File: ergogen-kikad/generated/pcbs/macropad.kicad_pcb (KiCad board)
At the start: 2 copper layers, 73.6 x 60.5 mm, 13 parts

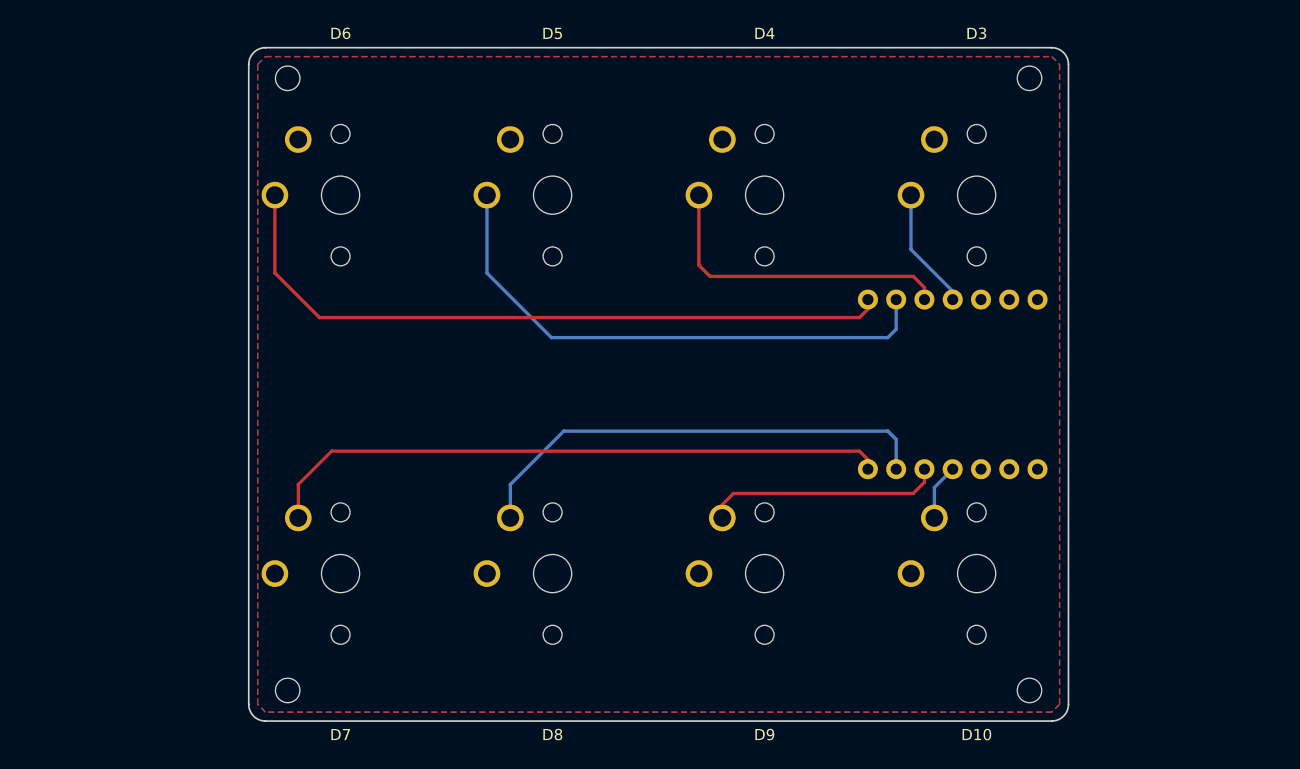
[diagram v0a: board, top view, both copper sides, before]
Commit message: Compact key rows and add controller-side keys through Ergogen
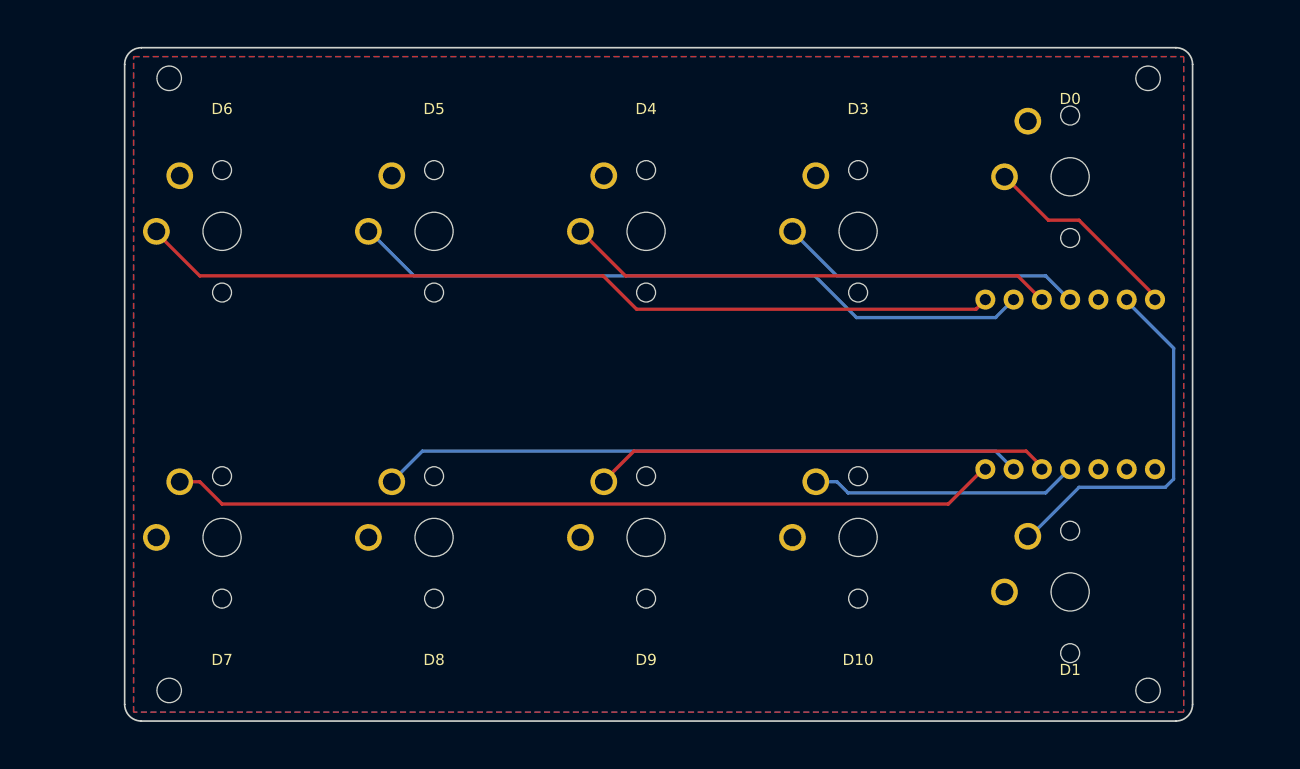
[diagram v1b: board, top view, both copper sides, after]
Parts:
- added S10: Choc v1 1U, PG1350_1U, F.Cu at (247.0, 167.2)
- added S9: Choc v1 1U, PG1350_1U, F.Cu at (247.0, 129.8)
- moved S1 11.1 mm to (170.8, 134.8)
- moved S2 11.1 mm to (189.8, 134.8)
- moved S3 11.1 mm to (208.9, 134.8)
- moved S5 11.1 mm to (170.8, 162.2)
- moved S6 11.1 mm to (189.8, 162.2)
- moved S7 11.1 mm to (208.9, 162.2)
- moved S4 11.1 mm to (227.9, 134.8)
- moved S8 11.1 mm to (227.9, 162.2)
- moved H1 10.7 mm to (166.0, 121.0)
- moved H2 10.7 mm to (254.0, 121.0)
- moved H3 10.7 mm to (166.0, 176.0)
- moved H4 10.7 mm to (254.0, 176.0)
- moved MCU1 10.5 mm to (247.0, 148.5)
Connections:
- MCU1 pad 1: (no net) -> D0
- MCU1 pad 2: (no net) -> D1
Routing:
- net D1: track 0.00 -> 33.2 mm
- net D9: track 21.4 -> 41.4 mm
- net D10: track 5.06 -> 24.6 mm
- net D0: track 0.00 -> 18.7 mm
- net D7: track 56.6 -> 74.6 mm
- net D3: track 10.9 -> 27.7 mm
- net D4: track 28.5 -> 44.3 mm
- net D8: track 42.6 -> 57.7 mm
- net D6: track 63.1 -> 78.0 mm
- net D5: track 49.2 -> 61.9 mm
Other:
- board size 73.6 x 60.5 mm -> 96 x 60.5 mm

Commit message: Align fifth-column caps with outer row edges
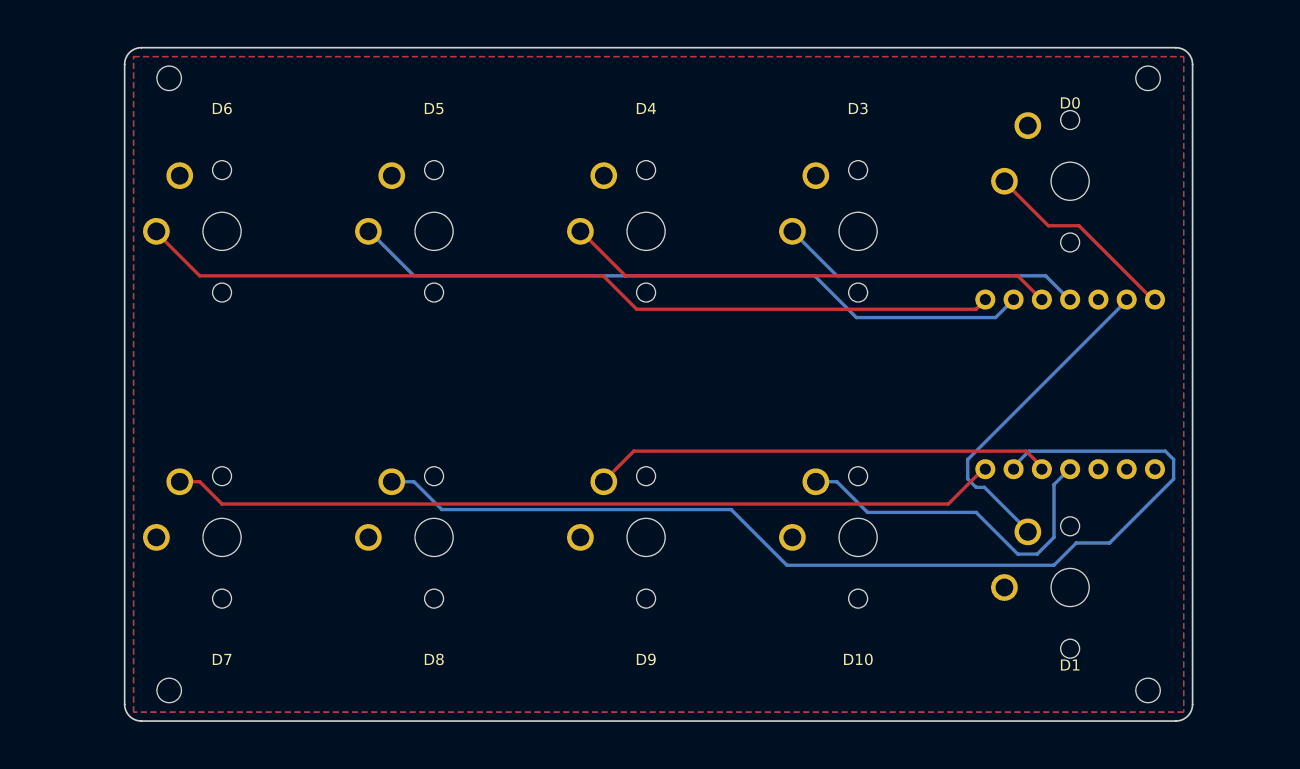
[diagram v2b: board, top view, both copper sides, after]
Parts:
- moved S10 0.40 mm to (247.0, 166.8)
- moved S9 0.40 mm to (247.0, 130.2)
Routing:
- net D8: track 57.7 -> 93.9 mm
- net D10: track 24.6 -> 31.9 mm
- net D1: track 33.2 -> 29.6 mm
- net D0: track 18.7 -> 18.1 mm

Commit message: Move mounts between switches and trim the board border
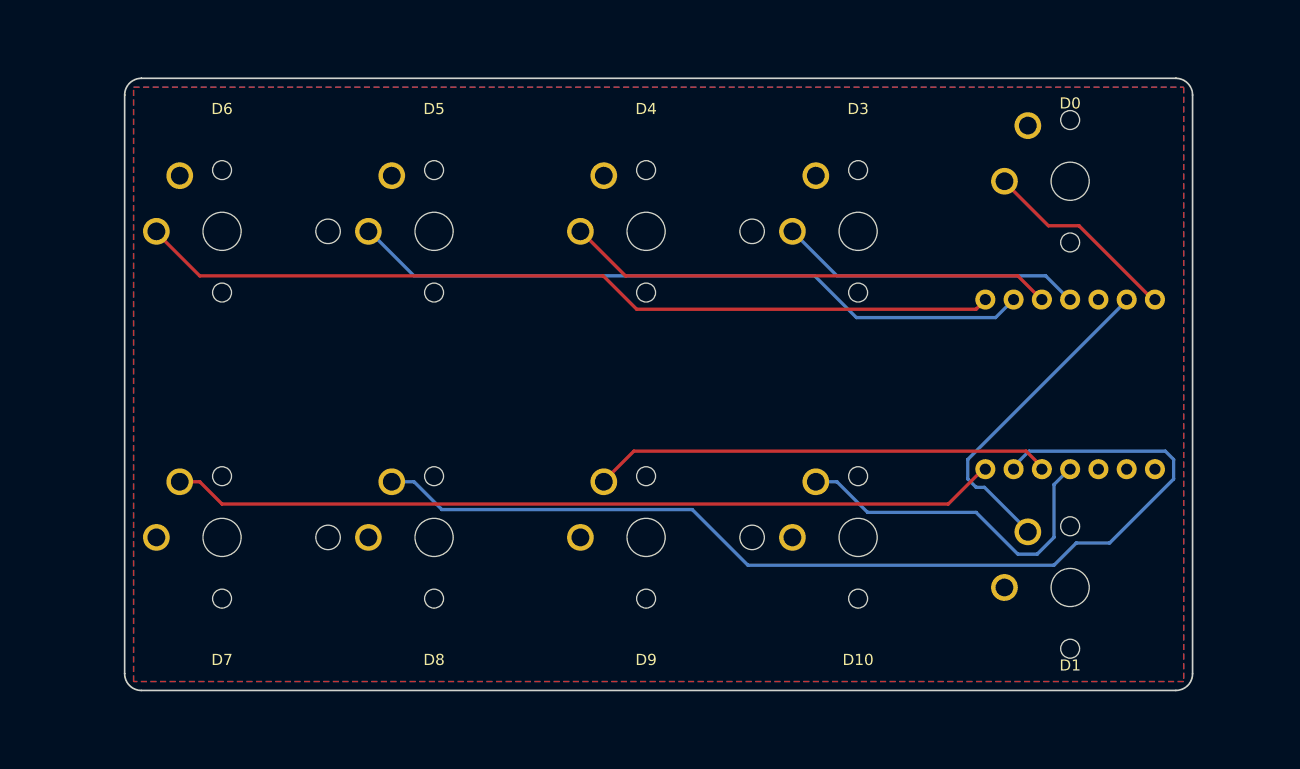
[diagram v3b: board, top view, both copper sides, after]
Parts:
- moved H2 38.1 mm to (218.4, 134.8)
- moved H4 38.1 mm to (218.4, 162.2)
- moved H1 19.8 mm to (180.3, 134.8)
- moved H3 19.8 mm to (180.3, 162.2)
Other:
- board size 96 x 60.5 mm -> 96 x 55 mm

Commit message: Add compact stacked memory LCD and regenerate matching carrier
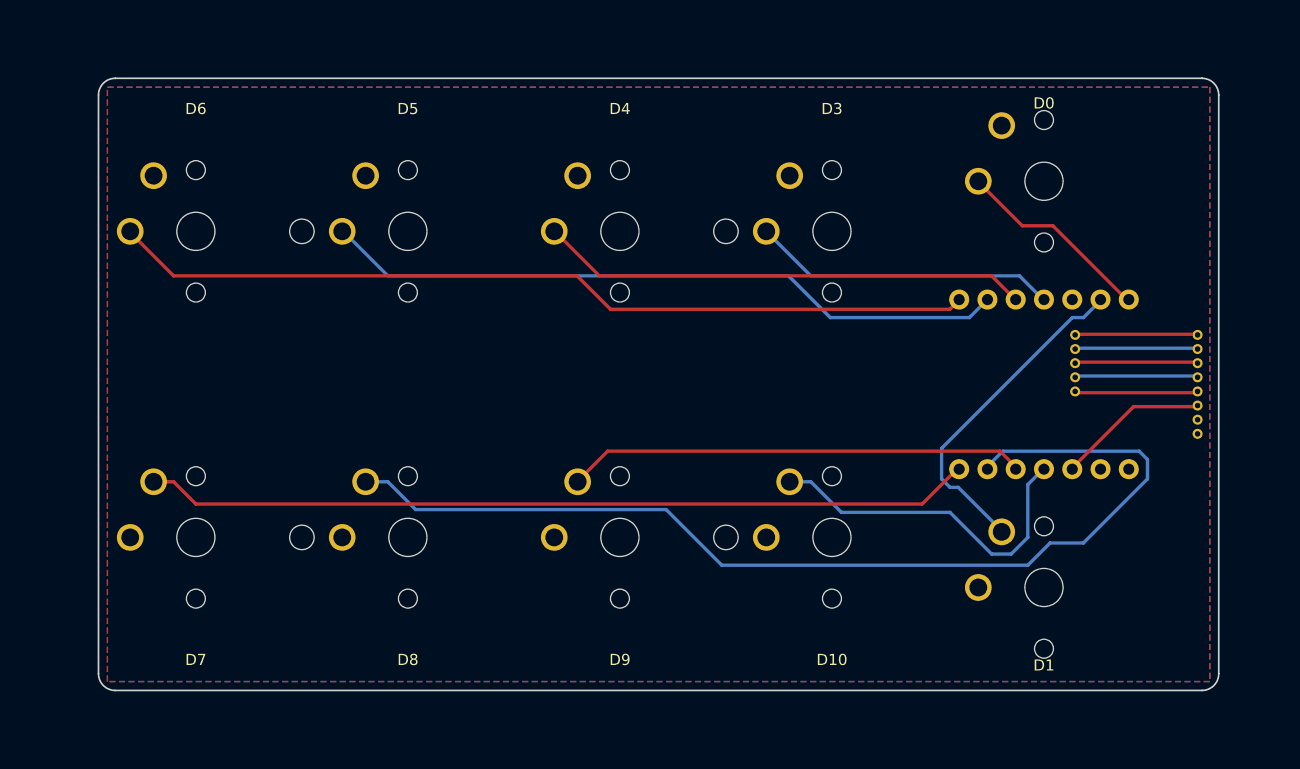
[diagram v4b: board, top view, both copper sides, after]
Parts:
- added LCD1: JDI LPM009M360A, JDI_LPM009M360A_Stack, F.Cu at (247.1, 148.5)
- added W1: Plus underside jumpers, XIAO_Plus_Underside_Wires, F.Cu at (247.4, 144.1)
- MCU1: value XIAO nRF52840 -> XIAO nRF52840 Plus
- moved H1 2.35 mm to (177.9, 134.8)
- moved H3 2.35 mm to (177.9, 162.2)
- moved S4 2.35 mm to (225.6, 134.8)
- moved S8 2.35 mm to (225.6, 162.2)
- moved H2 2.35 mm to (216.1, 134.8)
- moved H4 2.35 mm to (216.1, 162.2)
- moved MCU1 2.35 mm to (244.6, 148.5)
- moved S1 2.35 mm to (168.4, 134.8)
- moved S10 2.35 mm to (244.6, 166.8)
- moved S2 2.35 mm to (187.5, 134.8)
- moved S3 2.35 mm to (206.5, 134.8)
- moved S5 2.35 mm to (168.4, 162.2)
- moved S6 2.35 mm to (187.5, 162.2)
- moved S7 2.35 mm to (206.5, 162.2)
- moved S9 2.35 mm to (244.6, 130.2)
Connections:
- MCU1 pad 12: (no net) -> 3V3
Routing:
- net 3V3: track 0.00 -> 13.7 mm
- net LCD_EN: track 0.00 -> 11.2 mm
- net LCD_COM: track 0.00 -> 11.2 mm
- net LCD_CS: track 0.00 -> 11.2 mm
- net LCD_SI: track 0.00 -> 11.1 mm
- net LCD_CLK: track 0.00 -> 11.1 mm
- net D1: track 29.6 -> 30.2 mm
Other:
- board size 96 x 55 mm -> 100.6 x 55 mm

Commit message: Replace bare LCD with through-hole nice!view and nice!nano modules
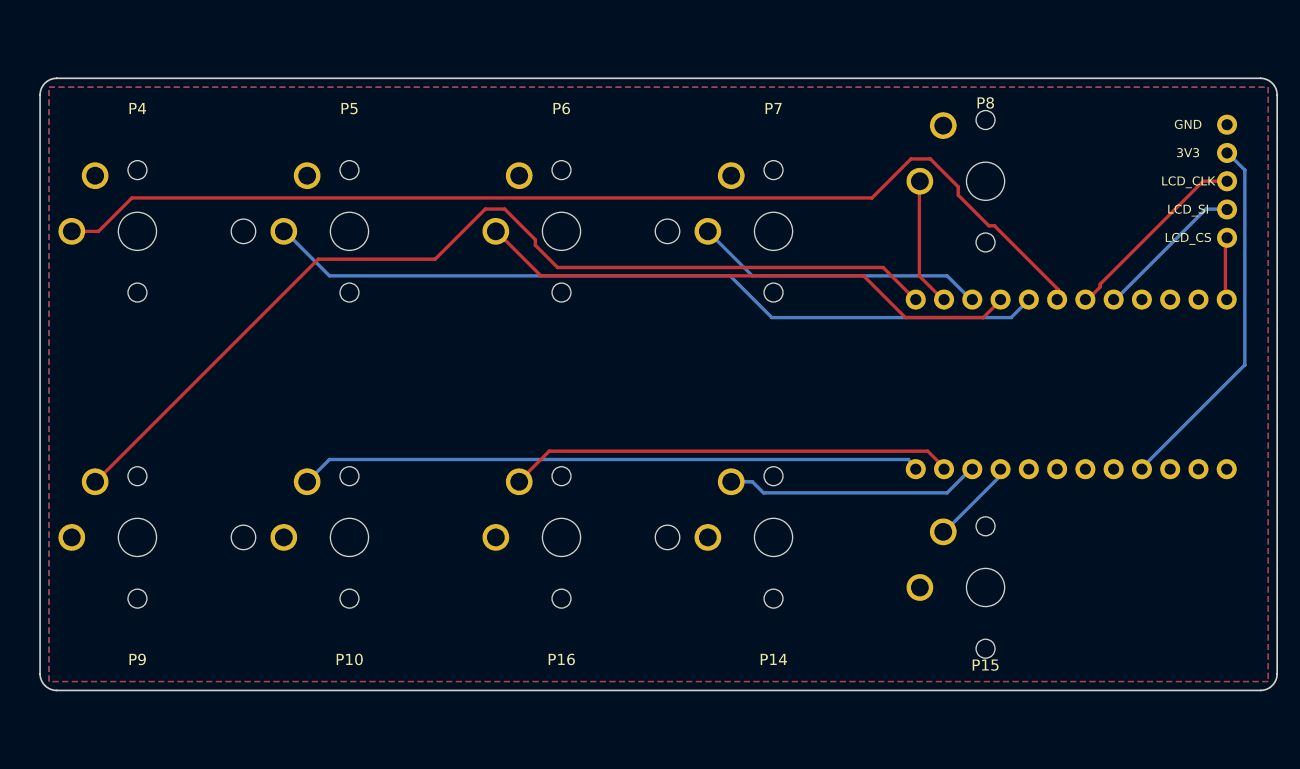
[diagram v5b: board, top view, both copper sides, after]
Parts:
- removed W1: Plus underside jumpers, XIAO_Plus_Underside_Wires
- LCD1: value JDI LPM009M360A -> nice!view; footprint JDI_LPM009M360A_Stack -> Nice_View_Wired_Module
- MCU1: value XIAO nRF52840 Plus -> nice!nano v2; footprint Seeed_XIAO_nRF52840 -> Nice_Nano_V2
- moved H1 5.25 mm to (172.7, 134.8)
- moved H2 5.25 mm to (210.8, 134.8)
- moved H3 5.25 mm to (172.7, 162.2)
- moved H4 5.25 mm to (210.8, 162.2)
- moved S1 5.25 mm to (163.2, 134.8)
- moved S10 5.25 mm to (239.4, 166.8)
- moved S2 5.25 mm to (182.2, 134.8)
- moved S3 5.25 mm to (201.3, 134.8)
- moved S4 5.25 mm to (220.3, 134.8)
- moved S5 5.25 mm to (163.2, 162.2)
- moved S6 5.25 mm to (182.2, 162.2)
- moved S7 5.25 mm to (201.3, 162.2)
- moved S8 5.25 mm to (220.3, 162.2)
- moved S9 5.25 mm to (239.4, 130.2)
- moved MCU1 2.45 mm to (247.1, 148.5)
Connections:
- net D6 renamed P4
- LCD1 pad 1: LCD_CLK -> GND
- LCD1 pad 2: LCD_SI -> 3V3
- LCD1 pad 3: LCD_CS -> LCD_CLK
- LCD1 pad 4: LCD_COM -> LCD_SI
- LCD1 pad 5: LCD_EN -> LCD_CS
- MCU1 pad 1: D0 -> LCD_CS
- MCU1 pad 10: D9 -> P7
- MCU1 pad 11: D10 -> P8
- MCU1 pad 12: 3V3 -> P9
- MCU1 pad 13: GND -> P10
- MCU1 pad 14: (no net) -> P16
- MCU1 pad 2: D1 -> (no net)
- MCU1 pad 3: (no net) -> GND
- MCU1 pad 4: D3 -> GND
- MCU1 pad 5: D4 -> LCD_SI
- MCU1 pad 6: D5 -> LCD_CLK
- MCU1 pad 8: D7 -> P5
- MCU1 pad 9: D8 -> P6
- S10 pad 1: D1 -> P15
- S2 pad 2: D5 -> P5
- S3 pad 2: D4 -> P6
- S4 pad 2: D3 -> P7
- S5 pad 1: D7 -> P9
- S6 pad 1: D8 -> P10
- S7 pad 1: D9 -> P16
- S8 pad 1: D10 -> P14
- S9 pad 2: D0 -> P8
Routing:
- net D8: track 93.9 -> 0.00 mm
- net P9: track 0.00 -> 87.8 mm
- net D7: track 74.6 -> 0.00 mm
- net P5: track 0.00 -> 70.8 mm
- net D5: track 61.9 -> 0.00 mm
- net P10: track 0.00 -> 56.0 mm
- net P6: track 0.00 -> 49.3 mm
- net D4: track 44.3 -> 0.00 mm
- net D9: track 41.4 -> 0.00 mm
- net P16: track 0.00 -> 40.2 mm
- net D10: track 31.9 -> 0.00 mm
- net D1: track 30.2 -> 0.00 mm
- net D3: track 27.7 -> 0.00 mm
- net P7: track 0.00 -> 26.5 mm
- net P14: track 0.00 -> 23.3 mm
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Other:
- board size 100.6 x 55 mm -> 111.1 x 55 mm

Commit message: Use landscape fifth-column caps and add right-side mounting pair
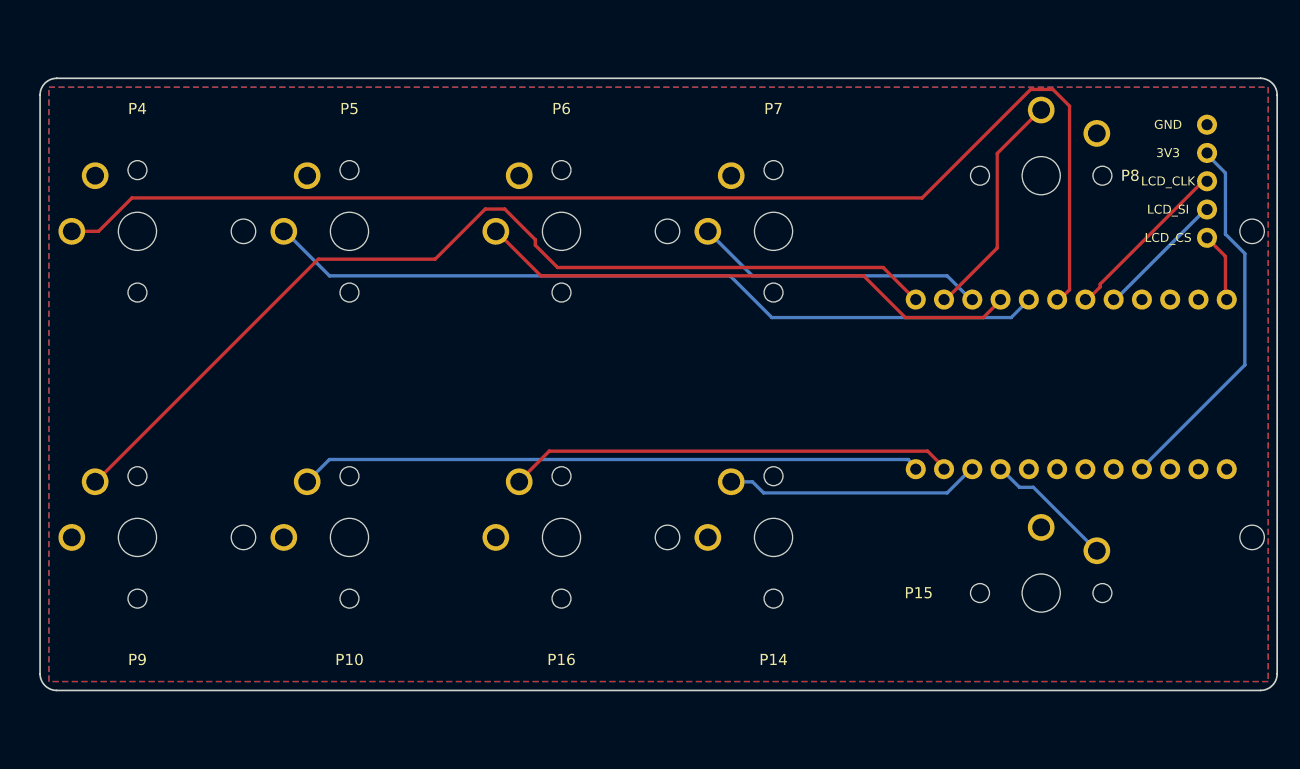
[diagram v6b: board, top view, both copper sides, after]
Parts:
- added H5: M2 mount, M2_Mount, F.Cu at (263.3, 134.8)
- added H6: M2 mount, M2_Mount, F.Cu at (263.3, 162.2)
- S10, S9: value Choc v1 1U -> Choc v1 1.5U; footprint PG1350_1U -> PG1350_1_5U
- moved S10 5.02 mm to (244.4, 167.2), turned to 0 degrees
- moved S9 5.02 mm to (244.4, 129.8), turned to 0 degrees
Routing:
- net P4: track 98.0 -> 113.8 mm
- net P8: track 11.9 -> 21.1 mm
- net P15: track 8.06 -> 12.1 mm
- net LCD_SI: track 13.9 -> 11.9 mm
- net LCD_CLK: track 17.6 -> 15.6 mm
- net 3V3: track 32.9 -> 33.8 mm
- net LCD_CS: track 6.16 -> 6.78 mm

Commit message: Add through-hole battery connector and top-facing power and reset controls
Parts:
- added BAT1: 301230 110mAh max 32.5x12.5x3.2, Protected_301230_Battery_Envelope, F.Cu at (191.8, 148.5)
- added J1: JST-PH B2B-PH-K-S, JST_PH_B2B_PH_K_Vertical, F.Cu at (261.4, 134.2)
- added PWR1: OS102011MS2QN1, CK_OS102011MS2QN1, F.Cu at (263.2, 167.2)
- added RST1: 6mm top-actuated tactile, SW_PUSH_6mm_H4_3mm, F.Cu at (261.3, 126.5)
- moved H5 33.5 mm to (229.8, 134.8)
- moved H6 33.5 mm to (229.8, 162.2)
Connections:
- MCU1 pad 22: (no net) -> RST
- MCU1 pad 24: (no net) -> VBAT
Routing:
- net LCD_CS: track 6.78 -> 206.5 mm
- net LCD_SI: track 11.9 -> 170.8 mm
- net LCD_CLK: track 15.6 -> 128.7 mm
- net BAT_POS: track 0.00 -> 38.0 mm
- net RST: track 0.00 -> 37.6 mm
- net 3V3: track 33.8 -> 11.4 mm
- net VBAT: track 0.00 -> 12.6 mm

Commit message: Reserve longer battery and export native KiCad assembly views
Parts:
- BAT1: value 301230 110mAh max 32.5x12.5x3.2 -> 301055 220mAh max 57.5x10.5x3.5; footprint Protected_301230_Battery_Envelope -> Protected_301055_Battery_Envelope
- J1: value JST-PH B2B-PH-K-S -> JST-PH S2B-PH-K-S; footprint JST_PH_B2B_PH_K_Vertical -> JST_PH_S2B_PH_K_Horizontal
- moved J1 105.7 mm to (156.7, 148.5), turned to 90 degrees
- moved BAT1 7.68 mm to (199.4, 148.5)
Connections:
- LCD1 pad 1: GND -> LCD_SI
- LCD1 pad 2: 3V3 -> LCD_CLK
- LCD1 pad 3: LCD_CLK -> 3V3
- LCD1 pad 4: LCD_SI -> GND
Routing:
- net LCD_SI: track 170.8 -> 27.4 mm
- net LCD_CLK: track 128.7 -> 41.5 mm
- net BAT_POS: track 38.0 -> 124.7 mm
- net LCD_CS: track 206.5 -> 181.1 mm
- net GND: track 0.00 -> 16.3 mm
- net 3V3: track 11.4 -> 13.6 mm
